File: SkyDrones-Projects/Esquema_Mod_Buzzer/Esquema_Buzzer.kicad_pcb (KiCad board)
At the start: 2 copper layers, 40 x 30 mm, 14 parts, among them J1 Conn_01x02_Pin, J2 Conn_01x03_Pin, Q1 BC337, U1 PC817, U2 MT3608

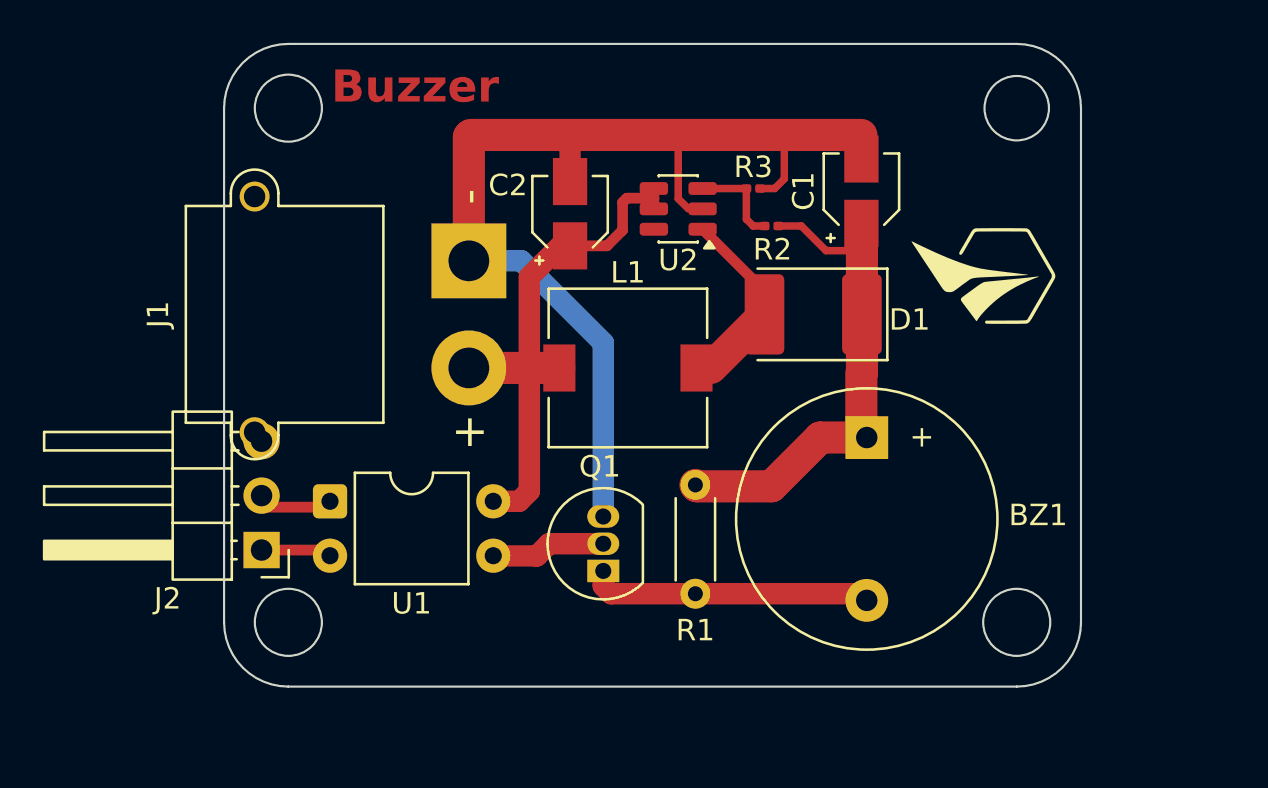
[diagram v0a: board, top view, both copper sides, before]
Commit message: [ADD] new project and upgrade
Upgrade - buzzer SD017
Nem Project - EC01 Sensor Universal
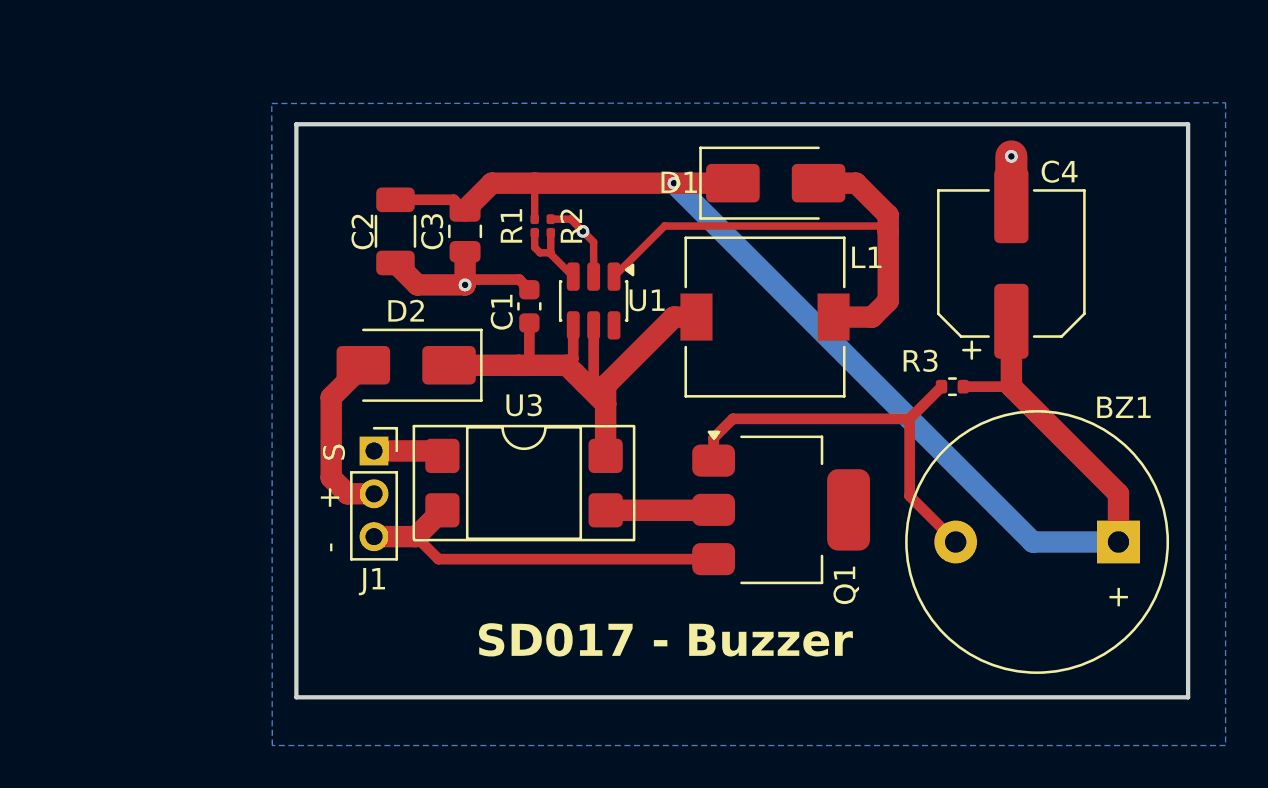
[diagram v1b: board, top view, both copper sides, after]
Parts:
- removed J2: Conn_01x03_Pin, Connector_PinHeader_2.54mm:PinHeader_1x03_P2.54mm_Horizontal
- removed U2: MT3608, Package_TO_SOT_SMD:SOT-23-6
- added C3: FCC0805X106K350FT 10uF, Capacitor_SMD:C_0805_2012Metric, F.Cu at (145.2, 93.8)
- added C4: PHV1JVB680MC10FVTSWP 68uF, Capacitor_SMD:CP_Elec_6.3x7.7, F.Cu at (170.8, 95.2)
- added D2: SS34, Diode_SMD:D_SMA, F.Cu at (142.5, 100.0)
- added U3: PC817, Package_DIP:DIP-4_W7.62mm_SMDSocket_SmallPads, F.Cu at (148.0, 105.5)
- C1: value 100uf -> CL10A226MQ8NRNC 22uF; footprint Capacitor_SMD:CP_Elec_3x5.3 -> Capacitor_SMD:C_0603_1608Metric
- C2: value 22uF -> CL31A107MQHNNNE 100uF; footprint Capacitor_SMD:CP_Elec_3x5.3 -> Capacitor_SMD:C_1206_3216Metric
- D1: footprint Diode_SMD:D_2114_3652Metric_Pad1.85x3.75mm_HandSolder -> Diode_SMD:D_SMA
- G***: moved to B.Cu
- J1: value Conn_01x02_Pin -> CUAV Servo Connector; footprint Amass:AMASS_XT30PW-M_1x02_P2.50mm_Horizontal -> Connector_PinSocket_2.00mm:PinSocket_1x03_P2.00mm_Vertical
- L1: value 10uH -> 22uH
- Q1: footprint Package_TO_SOT_THT:TO-92_Inline -> Package_TO_SOT_SMD:SOT-223
- R1: value 1k -> 90k; footprint Resistor_THT:R_Axial_DIN0204_L3.6mm_D1.6mm_P5.08mm_Horizontal -> Resistor_SMD:R_0201_0603Metric
- R2: value 10k -> 2.2k
- R3: value 390 -> 1k; footprint Resistor_SMD:R_0201_0603Metric -> Resistor_SMD:R_0402_1005Metric
- U1: value PC817 -> MT3608; footprint Package_DIP:DIP-4_W7.62mm -> Package_TO_SOT_SMD:SOT-23-6
- moved R1 18.7 mm to (148.5, 93.5)
- moved C1 16.4 mm to (148.2, 97.2)
- moved U1 15.5 mm to (151.2, 97.0), turned to -90 degrees
- moved G*** 13.2 mm to (159.2, 103.0), turned to 180 degrees
- moved R3 13.1 mm to (168.0, 101.0), turned to 0 degrees
- moved BZ1 12.7 mm to (175.8, 108.2), turned to 180 degrees
- moved R2 10.3 mm to (149.2, 93.5), turned to -90 degrees
- moved J1 9.92 mm to (141.0, 104.0), turned to 0 degrees
- moved Q1 8.78 mm to (160.0, 106.8), turned to 0 degrees
- moved C2 8.19 mm to (142.0, 93.8), turned to -90 degrees
- moved L1 6.83 mm to (159.2, 97.8)
- moved D1 6.37 mm to (159.8, 91.5), turned to 0 degrees
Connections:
- C1 pad 1: Net-(BZ1-+) -> /5V-CUAV
- C2 pad 1: Net-(J1-Pin_2) -> Net-(BZ1-+)
- J1 pad 1: GND -> Net-(J1-Pin_1)
- J1 pad 2: Net-(J1-Pin_2) -> Net-(D2-A)
- L1 pad 1: Net-(J1-Pin_2) -> /5V-CUAV
- R1 pad 1: Net-(BZ1--) -> Net-(U1-FB)
- R2 pad 1: Net-(U2-FB) -> GND
- R2 pad 2: Net-(BZ1-+) -> Net-(U1-FB)
- R3 pad 1: GND -> Net-(BZ1--)
- R3 pad 2: Net-(U2-FB) -> Net-(BZ1-+)
- U1 pad 1: Net-(J2-Pin_3) -> Net-(D1-A)
- U1 pad 2: Net-(J2-Pin_1) -> GND
- U1 pad 3: Net-(Q1-B) -> Net-(U1-FB)
- U1 pad 4: Net-(J1-Pin_2) -> /5V-CUAV
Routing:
- net Net-(BZ1-+): track 23.9 -> 60.9 mm, vias 0 -> 1
- net Net-(J1-Pin_2): track 25.2 -> 0.00 mm
- net /5V-CUAV: track 0.00 -> 23.9 mm
- net GND: track 51.2 -> 32.8 mm, vias 0 -> 3
- net Net-(D1-A): track 10.5 -> 24.6 mm
- net Net-(D2-A): track 0.00 -> 8.18 mm
- net Net-(BZ1--): track 13.3 -> 19.3 mm
- net Net-(U2-FB): track 4.46 -> 0.00 mm
- net Net-(U1-FB): track 0.00 -> 4.01 mm
- net Net-(J2-Pin_3): track 3.31 -> 0.00 mm
- net Net-(J2-Pin_1): track 3.30 -> 0.00 mm
- net Net-(J1-Pin_1): track 0.00 -> 3.29 mm
- added copper zone on B.Cu, net GND
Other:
- board size 40 x 30 mm -> 41.6 x 26.8 mm
- board text added: "+"
- board text added: "-"
- board text added: "S"
- board text added: "SD017 - Buzzer"
- board text removed: "Buzzer"
